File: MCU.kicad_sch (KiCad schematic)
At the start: 32 parts, among them J5 Conn_01x05, U7 NRF5340-QKAA-AB0-R, Y1 32MHz, Y2 32.768 KHz

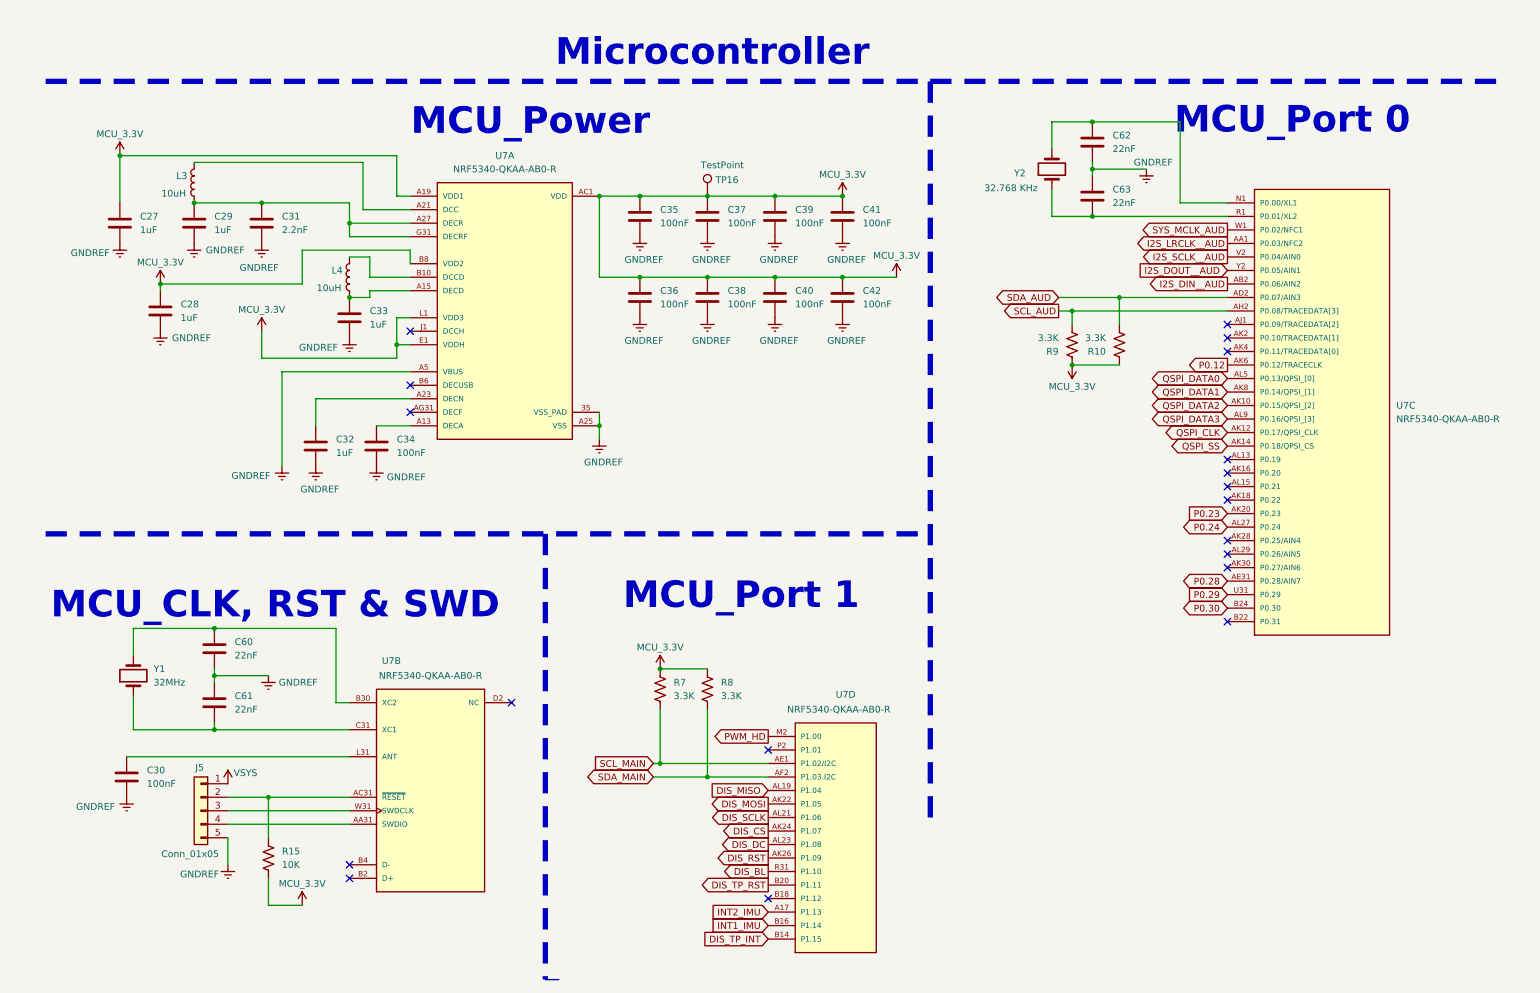
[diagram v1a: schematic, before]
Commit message: Updated capcitors value of XL1 and XL2
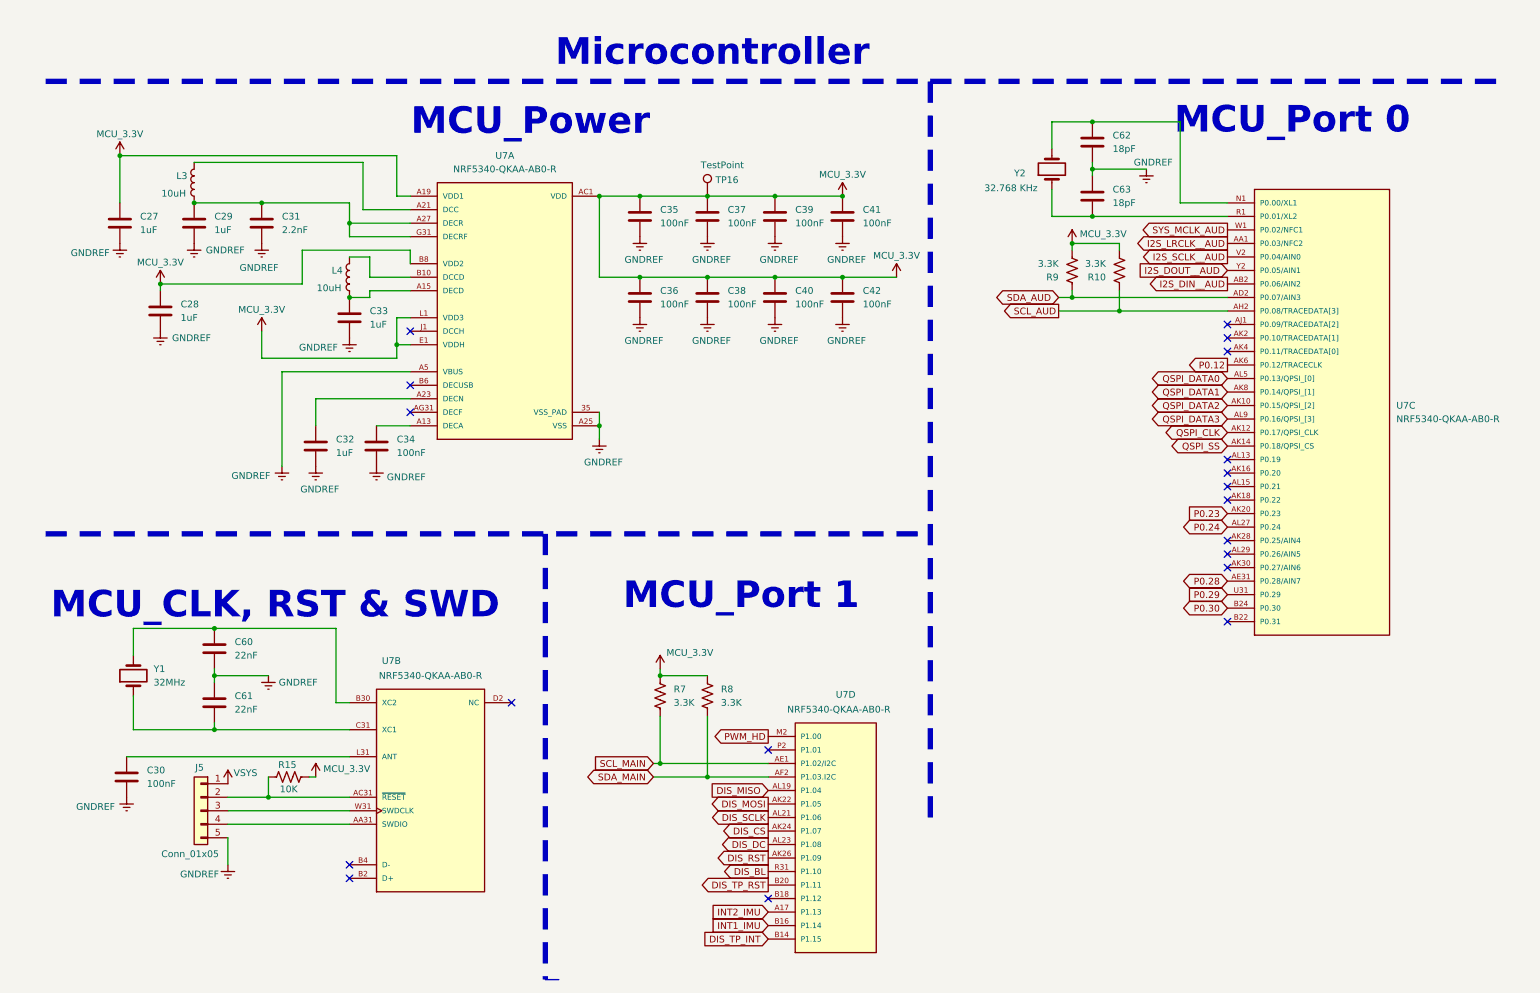
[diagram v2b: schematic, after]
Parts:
- C62, C63: value 22nF -> 18pF
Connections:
- net MCU_3.3V: now also R10.2, R9.2; no longer R10.1, R9.1
- net SCL_AUD: now also R10.1; no longer R9.2
- net SDA_AUD: now also R9.1; no longer R10.2
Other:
- moved on the sheet: R10, R15, R7, R8, R9

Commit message: updated version
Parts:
- C60, C61: value 22nF -> 12pF
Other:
- moved on the sheet: C30, C60, C61, C62, C63, J5, R10, R15, R7, R8, R9, U7B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
